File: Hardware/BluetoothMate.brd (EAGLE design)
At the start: 44.5 x 16.5 mm, 27 parts, among them Q1 MOSFET-NCHANNELSMD, Q2 MOSFET-NCHANNELSMD, U1 BLUETOOTH-RN41, U3 V_REG_LDOSMD

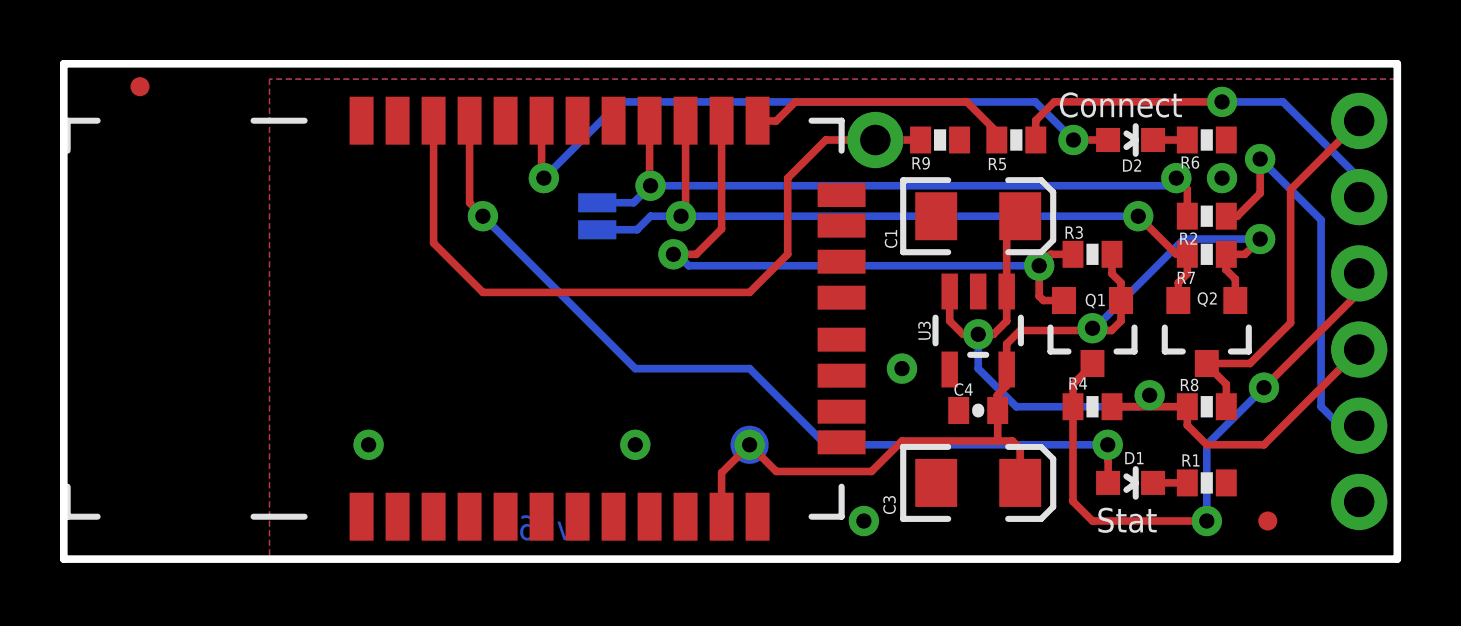
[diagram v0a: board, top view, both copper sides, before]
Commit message: Updated Caps/Res to 0603 packages
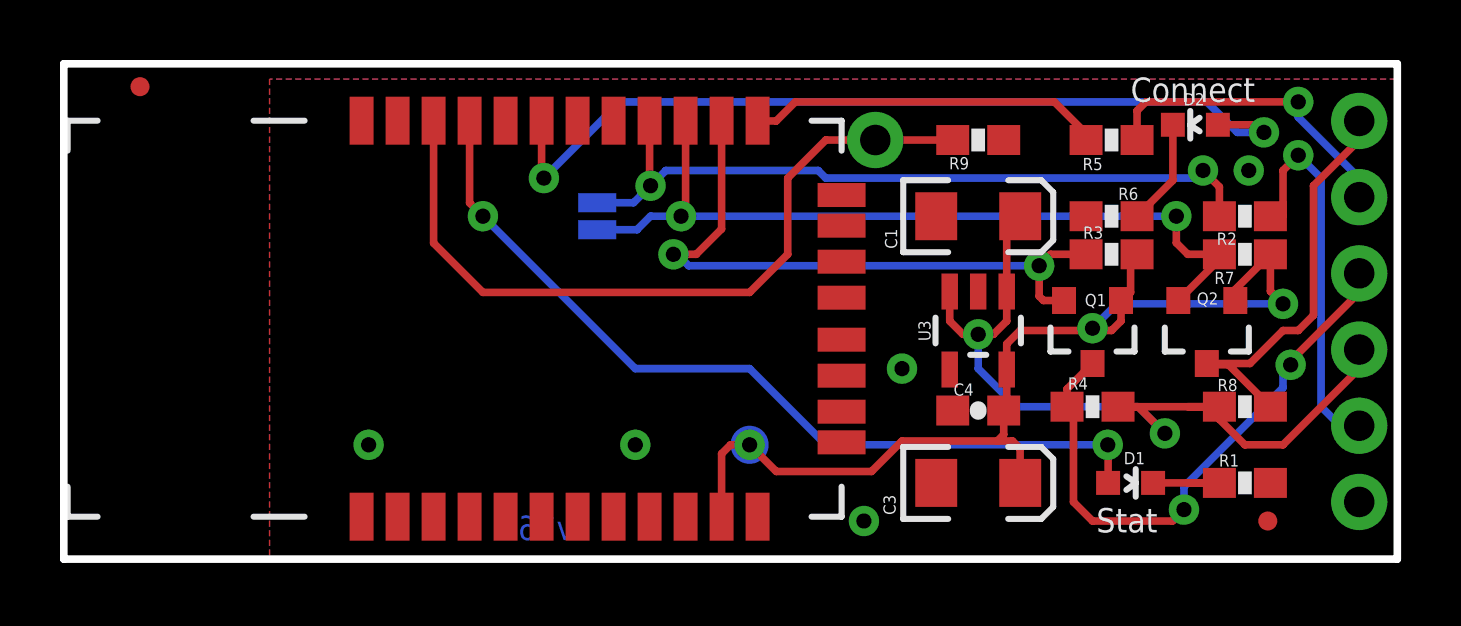
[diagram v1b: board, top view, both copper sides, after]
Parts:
- C4: device SparkFun:0402-CAP -> SparkFun:0603-CAP
- R1, R2, R3, R4, R5, R6, R7, R8, R9: device SparkFun:0402-RES -> SparkFun:0603-RES
- moved R6 4.07 mm to (34.9, 11.4), turned to 180 degrees
- moved R5 3.17 mm to (34.9, 14.0)
- moved D2 2.22 mm to (37.7, 14.5), turned to 90 degrees
- moved R9 1.27 mm to (30.5, 14.0)
- moved R1 1.27 mm to (39.4, 2.54)
- moved R2 1.27 mm to (39.4, 11.4)
- moved R7 1.27 mm to (39.4, 10.2)
- moved R8 1.27 mm to (39.4, 5.08)
- moved R3 0.63 mm to (34.9, 10.2)
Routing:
- net N$2: track 22.3 -> 29.1 mm
- net VCC: track 25.3 -> 28.9 mm
- net RX: track 8.92 -> 11.9 mm
- net RX_5V: track 13.4 -> 10.5 mm
- net D2: track 1.16 -> 3.54 mm
- net D1: track 1.16 -> 3.27 mm
- net RTS: track 25.3 -> 27.3 mm
- net CTS: track 23.2 -> 24.8 mm
- net RTS_5V: track 12.7 -> 14.1 mm
- net 3.3V: track 33.7 -> 34.9 mm
- net PIO4: track 24.6 -> 25.7 mm

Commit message: Additional updates to layout
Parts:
- removed JP4: FIDUCIAL1X2.5, abes:FIDUCIAL-1X2.5
- moved D2 1.73 mm to (39.4, 14.0)
- moved Q2 1.27 mm to (39.4, 7.62)
- moved R4 1.08 mm to (35.1, 4.32)
- moved R8 0.76 mm to (39.4, 4.32)
- moved C4 0.64 mm to (30.5, 4.32)
- moved C3 0.64 mm to (30.5, 1.91)
- moved D1 0.64 mm to (35.6, 1.91)
- moved R1 0.64 mm to (39.4, 1.91)
- moved R2 0.63 mm to (39.4, 12.1)
- moved R6 0.63 mm to (34.9, 12.1)
- moved Q1 0.63 mm to (34.9, 7.62)
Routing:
- net TX_5V: track 19.6 -> 16.2 mm
- net 3.3V: track 34.9 -> 31.7 mm, vias 3 -> 1
- net VCC: track 28.9 -> 26.7 mm
- net RX_5V: track 10.5 -> 12.7 mm
- net RTS_5V: track 14.1 -> 12.3 mm
- net RTS: track 27.3 -> 26.3 mm
- net CTS_5V: track 12.9 -> 11.9 mm
- net D1: track 3.27 -> 2.42 mm
- net CTS: track 24.8 -> 24.2 mm
- net GND: vias 5 -> 4

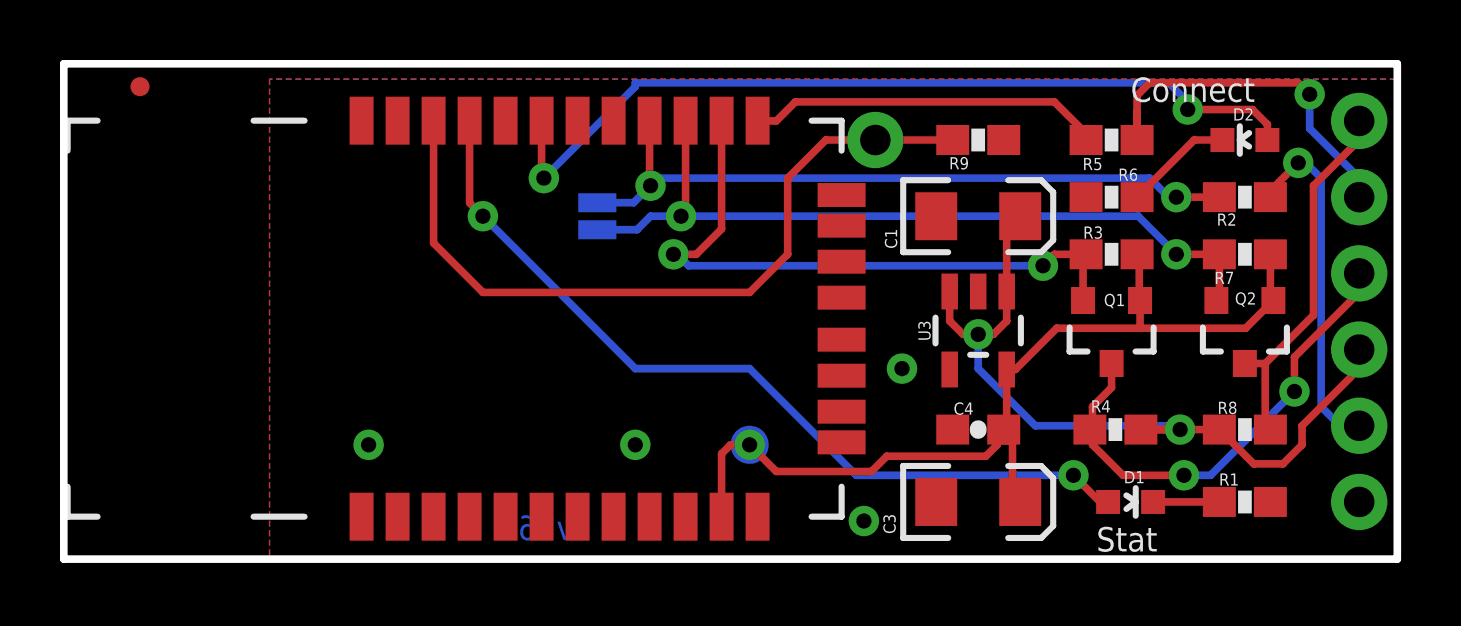
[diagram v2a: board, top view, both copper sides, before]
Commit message: Fixed additional layout issues
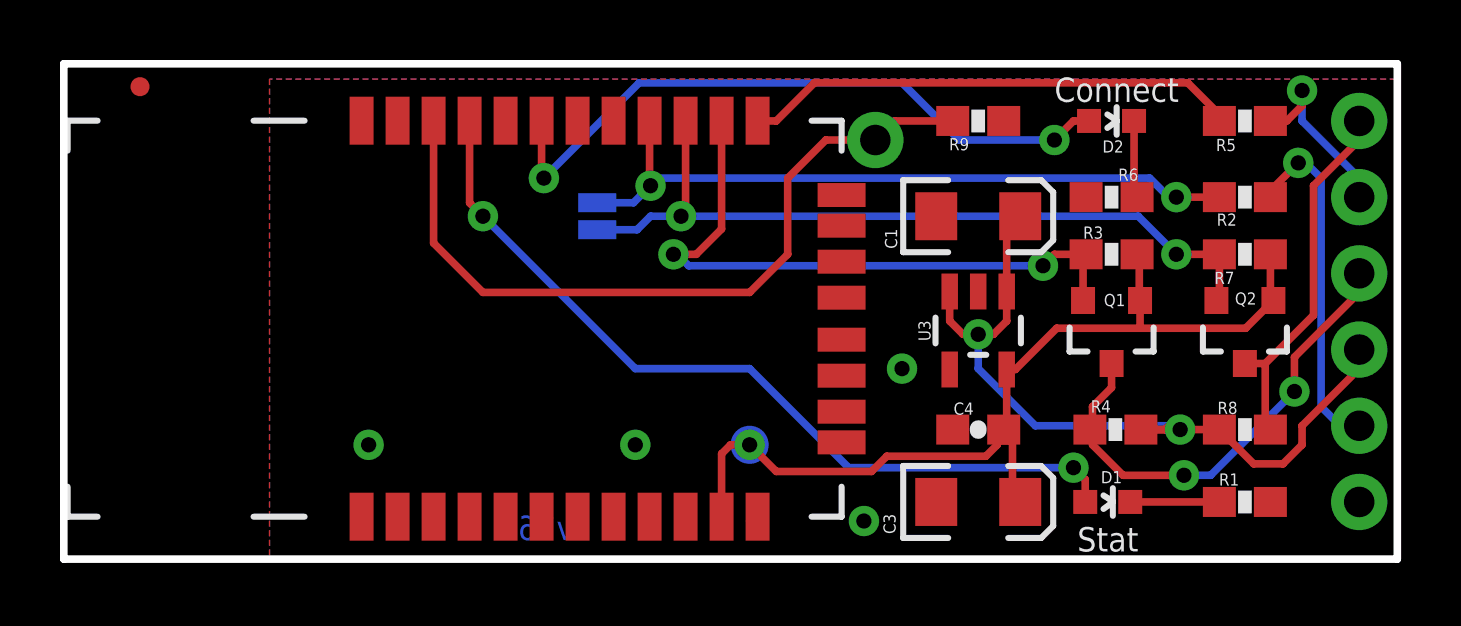
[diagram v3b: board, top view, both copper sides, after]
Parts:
- moved D2 4.49 mm to (34.9, 14.6), turned to 270 degrees
- moved R5 4.49 mm to (39.4, 14.6)
- moved D1 0.76 mm to (34.8, 1.91)
- moved R9 0.63 mm to (30.5, 14.6)
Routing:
- net RX_5V: track 12.7 -> 6.33 mm
- net N$2: track 28.7 -> 22.5 mm
- net RX: track 11.9 -> 16.6 mm
- net D2: track 3.63 -> 2.58 mm
- net D1: track 2.42 -> 3.19 mm
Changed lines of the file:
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@@
 <text x="41.656" y="3.937" size="1.016" layer="22" font="vector" ratio="15" rot="MR0">CTS-I</text>
 <text x="41.656" y="11.557" size="1.016" layer="22" font="vector" ratio="15" rot="MR0">RX-I</text>
-<text x="34.417" y="0.254" size="0.8128" layer="21" font="vector" ratio="15">Stat</text>
-<text x="35.56" y="15.24" size="0.8128" layer="21" font="vector" ratio="15">Connect</text>
+<text x="33.782" y="0.254" size="0.8128" layer="21" font="vector" ratio="15">Stat</text>
+<text x="33.02" y="15.24" size="0.8128" layer="21" font="vector" ratio="15">Connect</text>
 <text x="25.781" y="13.462" size="1.016" layer="22" font="vector" ratio="15" rot="MR0">PIO6</text>
 <text x="17.018" y="0.635" size="0.8128" layer="16" font="vector" ratio="25" rot="MR0">v16</text>
@@
 <attribute name="VALUE" x="36.1823" y="5.2832" size="0.4064" layer="27" rot="R180"/>
 </element>
-<element name="R5" library="SparkFun" package="0603-RES" value="10K" x="34.925" y="13.97" smashed="yes">
-<attribute name="NAME" x="33.9598" y="12.9667" size="0.4064" layer="25"/>
-<attribute name="VALUE" x="34.9123" y="12.9794" size="0.4064" layer="27"/>
-</element>
-<element name="D2" library="SparkFun" package="LED-0603" value="Green" x="39.37" y="13.97" smashed="yes" rot="R90">
-<attribute name="NAME" x="39.6748" y="15.0241" size="0.4064" layer="25" rot="R180"/>
-<attribute name="VALUE" x="40.132" y="15.0241" size="0.4064" layer="27" ratio="12" rot="R180"/>
+<element name="R5" library="SparkFun" package="0603-RES" value="10K" x="39.37" y="14.605" smashed="yes">
+<attribute name="NAME" x="38.4048" y="13.6017" size="0.4064" layer="25"/>
+<attribute name="VALUE" x="39.3573" y="13.6144" size="0.4064" layer="27"/>
+</element>
+<element name="D2" library="SparkFun" package="LED-0603" value="Green" x="34.925" y="14.605" smashed="yes" rot="R270">
+<attribute name="NAME" x="34.6202" y="13.5509" size="0.4064" layer="25"/>
+<attribute name="VALUE" x="34.163" y="13.5509" size="0.4064" layer="27" ratio="12"/>
 </element>
 <element name="R6" library="SparkFun" package="0603-RES" value="330" x="34.925" y="12.065" smashed="yes" rot="R180">
@@
 <element name="SJ1" library="SparkFun" package="SJ_2S-NO" value="SOLDERJUMPERNO" x="17.78" y="11.43" rot="MR90"/>
 <element name="U1" library="SparkFun-RF" package="RN41" value="BLUETOOTH-RN41" x="16.526" y="8.014"/>
-<element name="D1" library="SparkFun" package="LED-0603" value="Red" x="35.56" y="1.905" smashed="yes" rot="R270">
-<attribute name="NAME" x="35.3314" y="2.5273" size="0.4064" layer="25"/>
-<attribute name="VALUE" x="35.179" y="2.6035" size="0.4064" layer="27" ratio="12"/>
-</element>
-<element name="R9" library="SparkFun" package="0603-RES" value="10K" x="30.48" y="13.97" smashed="yes" rot="R180">
-<attribute name="NAME" x="30.1752" y="13.3985" size="0.4064" layer="25" rot="R180"/>
-<attribute name="VALUE" x="31.4833" y="13.4112" size="0.4064" layer="27" rot="R180"/>
+<element name="D1" library="SparkFun" package="LED-0603" value="Red" x="34.798" y="1.905" smashed="yes" rot="R270">
+<attribute name="NAME" x="34.5694" y="2.5273" size="0.4064" layer="25"/>
+<attribute name="VALUE" x="34.417" y="2.6035" size="0.4064" layer="27" ratio="12"/>
+</element>
+<element name="R9" library="SparkFun" package="0603-RES" value="10K" x="30.48" y="14.605" smashed="yes" rot="R180">
+<attribute name="NAME" x="30.1752" y="14.0335" size="0.4064" layer="25" rot="R180"/>
+<attribute name="VALUE" x="31.4833" y="14.0462" size="0.4064" layer="27" rot="R180"/>
 </element>
 <element name="JP2" library="SparkFun" package="1X01NS" value="M01SMDNS" x="27.051" y="13.97"/>
@@
 <contactref element="R1" pad="1"/>
 <contactref element="D1" pad="C"/>
-<wire x1="36.31" y1="1.905" x2="38.52" y2="1.905" width="0.254" layer="1"/>
+<wire x1="35.548" y1="1.905" x2="38.52" y2="1.905" width="0.254" layer="1"/>
 <wire x1="38.735" y1="1.905" x2="38.52" y2="1.905" width="0.254" layer="1"/>
 </signal>
@@
 <contactref element="R5" pad="1"/>
 <contactref element="U1" pad="13"/>
-<wire x1="24.384" y1="15.24" x2="33.02" y2="15.24" width="0.254" layer="1"/>
-<wire x1="23.749" y1="14.605" x2="24.384" y2="15.24" width="0.254" layer="1"/>
 <wire x1="23.135" y1="14.605" x2="23.749" y2="14.605" width="0.254" layer="1"/>
 <wire x1="23.126" y1="14.614" x2="23.135" y2="14.605" width="0.254" layer="1"/>
-<wire x1="34.075" y1="13.97" x2="34.075" y2="14.185" width="0.254" layer="1"/>
-<wire x1="34.075" y1="14.185" x2="33.02" y2="15.24" width="0.254" layer="1"/>
+<wire x1="38.52" y1="14.605" x2="38.52" y2="14.82" width="0.254" layer="1"/>
+<wire x1="38.52" y1="14.82" x2="37.465" y2="15.875" width="0.254" layer="1"/>
+<wire x1="37.465" y1="15.875" x2="25.019" y2="15.875" width="0.254" layer="1"/>
+<wire x1="25.019" y1="15.875" x2="23.749" y2="14.605" width="0.254" layer="1"/>
 </signal>
 <signal name="RX_5V">
 <contactref element="R5" pad="2"/>
 <contactref element="JP3" pad="2"/>
-<via x="41.529" y="15.494" extent="1-16" drill="0.508"/>
-<wire x1="35.775" y1="13.97" x2="35.775" y2="14.947" width="0.254" layer="1"/>
-<wire x1="41.529" y1="15.494" x2="41.529" y2="14.351" width="0.254" layer="16"/>
-<wire x1="41.529" y1="14.351" x2="43.18" y2="12.7" width="0.254" layer="16"/>
+<via x="41.275" y="15.621" extent="1-16" drill="0.508"/>
+<wire x1="41.275" y1="14.605" x2="43.18" y2="12.7" width="0.254" layer="16"/>
 <wire x1="43.18" y1="12.7" x2="43.18" y2="12.065" width="0.254" layer="16"/>
-<wire x1="35.775" y1="13.97" x2="35.775" y2="15.455" width="0.254" layer="1"/>
-<wire x1="35.775" y1="15.455" x2="36.195" y2="15.875" width="0.254" layer="1"/>
-<wire x1="36.195" y1="15.875" x2="41.148" y2="15.875" width="0.254" layer="1"/>
-<wire x1="41.148" y1="15.875" x2="41.529" y2="15.494" width="0.254" layer="1"/>
+<wire x1="40.22" y1="14.605" x2="40.22" y2="14.82" width="0.254" layer="1"/>
+<wire x1="41.275" y1="15.621" x2="41.275" y2="14.605" width="0.254" layer="16"/>
+<wire x1="40.22" y1="14.605" x2="40.767" y2="14.605" width="0.254" layer="1"/>
+<wire x1="40.767" y1="14.605" x2="41.275" y2="15.113" width="0.254" layer="1"/>
+<wire x1="41.275" y1="15.113" x2="41.275" y2="15.621" width="0.254" layer="1"/>
 </signal>
 <signal name="VCC">
@@
 <contactref element="D2" pad="C"/>
 <contactref element="R6" pad="1"/>
-<wire x1="37.68" y1="13.97" x2="35.775" y2="12.065" width="0.254" layer="1"/>
-<wire x1="38.62" y1="13.97" x2="37.68" y2="13.97" width="0.254" layer="1"/>
+<wire x1="35.675" y1="14.605" x2="35.675" y2="12.165" width="0.254" layer="1"/>
+<wire x1="35.675" y1="12.165" x2="35.775" y2="12.065" width="0.254" layer="1"/>
 </signal>
 <signal name="N$1">
@@
 <wire x1="13.526" y1="11.874" x2="13.526" y2="14.614" width="0.254" layer="1"/>
 <wire x1="13.97" y1="11.43" x2="13.526" y2="11.874" width="0.254" layer="1"/>
-<wire x1="22.86" y1="6.35" x2="26.416" y2="2.794" width="0.254" layer="16"/>
 <wire x1="19.05" y1="6.35" x2="22.86" y2="6.35" width="0.254" layer="16"/>
-<via x="33.655" y="2.794" extent="1-16" drill="0.508"/>
+<via x="33.655" y="3.048" extent="1-16" drill="0.508"/>
 <via x="13.97" y="11.43" extent="1-16" drill="0.508"/>
-<wire x1="34.81" y1="1.905" x2="34.544" y2="1.905" width="0.254" layer="1"/>
-<wire x1="34.544" y1="1.905" x2="33.655" y2="2.794" width="0.254" layer="1"/>
-<wire x1="33.655" y1="2.794" x2="26.416" y2="2.794" width="0.254" layer="16"/>
+<wire x1="33.655" y1="3.048" x2="26.162" y2="3.048" width="0.254" layer="16"/>
+<wire x1="26.162" y1="3.048" x2="22.86" y2="6.35" width="0.254" layer="16"/>
+<wire x1="34.048" y1="1.905" x2="34.048" y2="2.655" width="0.254" layer="1"/>
+<wire x1="34.048" y1="2.655" x2="33.655" y2="3.048" width="0.254" layer="1"/>
 </signal>
 <signal name="N$2">
@@
 <wire x1="15.926" y1="14.614" x2="15.926" y2="12.776" width="0.254" layer="1"/>
 <wire x1="15.926" y1="12.776" x2="16.002" y2="12.7" width="0.254" layer="1"/>
-<wire x1="16.002" y1="12.7" x2="19.05" y2="15.748" width="0.254" layer="16"/>
-<via x="37.465" y="14.986" extent="1-16" drill="0.508"/>
 <via x="16.002" y="12.7" extent="1-16" drill="0.508"/>
-<wire x1="36.83" y1="15.875" x2="19.05" y2="15.875" width="0.254" layer="16"/>
-<wire x1="19.05" y1="15.875" x2="19.05" y2="15.748" width="0.254" layer="16"/>
-<wire x1="37.465" y1="14.986" x2="37.465" y2="15.24" width="0.254" layer="16"/>
-<wire x1="37.465" y1="15.24" x2="36.83" y2="15.875" width="0.254" layer="16"/>
-<wire x1="40.12" y1="13.97" x2="40.12" y2="14.49" width="0.254" layer="1"/>
-<wire x1="37.465" y1="14.986" x2="39.624" y2="14.986" width="0.254" layer="1"/>
-<wire x1="39.624" y1="14.986" x2="40.12" y2="14.49" width="0.254" layer="1"/>
+<wire x1="34.175" y1="14.605" x2="33.655" y2="14.605" width="0.254" layer="1"/>
+<wire x1="33.655" y1="14.605" x2="33.02" y2="13.97" width="0.254" layer="1"/>
+<via x="33.02" y="13.97" extent="1-16" drill="0.508"/>
+<wire x1="33.02" y1="13.97" x2="29.845" y2="13.97" width="0.254" layer="16"/>
+<wire x1="29.845" y1="13.97" x2="27.94" y2="15.875" width="0.254" layer="16"/>
+<wire x1="27.94" y1="15.875" x2="19.177" y2="15.875" width="0.254" layer="16"/>
+<wire x1="19.177" y1="15.875" x2="16.002" y2="12.7" width="0.254" layer="16"/>
 </signal>
 <signal name="PIO4">
@@
 <wire x1="24.13" y1="12.7" x2="25.4" y2="13.97" width="0.254" layer="1"/>
 <wire x1="25.4" y1="13.97" x2="27.051" y2="13.97" width="0.254" layer="1"/>
-<wire x1="27.051" y1="13.97" x2="29.63" y2="13.97" width="0.254" layer="1"/>
+<wire x1="29.63" y1="14.605" x2="27.686" y2="14.605" width="0.254" layer="1"/>
+<wire x1="27.686" y1="14.605" x2="27.051" y2="13.97" width="0.254" layer="1"/>
 </signal>
 </signals>
